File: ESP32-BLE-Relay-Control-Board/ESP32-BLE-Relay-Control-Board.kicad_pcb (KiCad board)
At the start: 2 copper layers, 37 x 90 mm, 37 parts, among them J1 Screw_Terminal_01x02, J2 Screw_Terminal_01x02, J3 Screw_Terminal_01x02, J4 Screw_Terminal_01x02, J5 Conn_01x06_Female, K1 SANYOU_SRD_Form_C, K2 SANYOU_SRD_Form_C, Q1 BC817, Q2 BC817, U1 ESP32-WROOM-32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

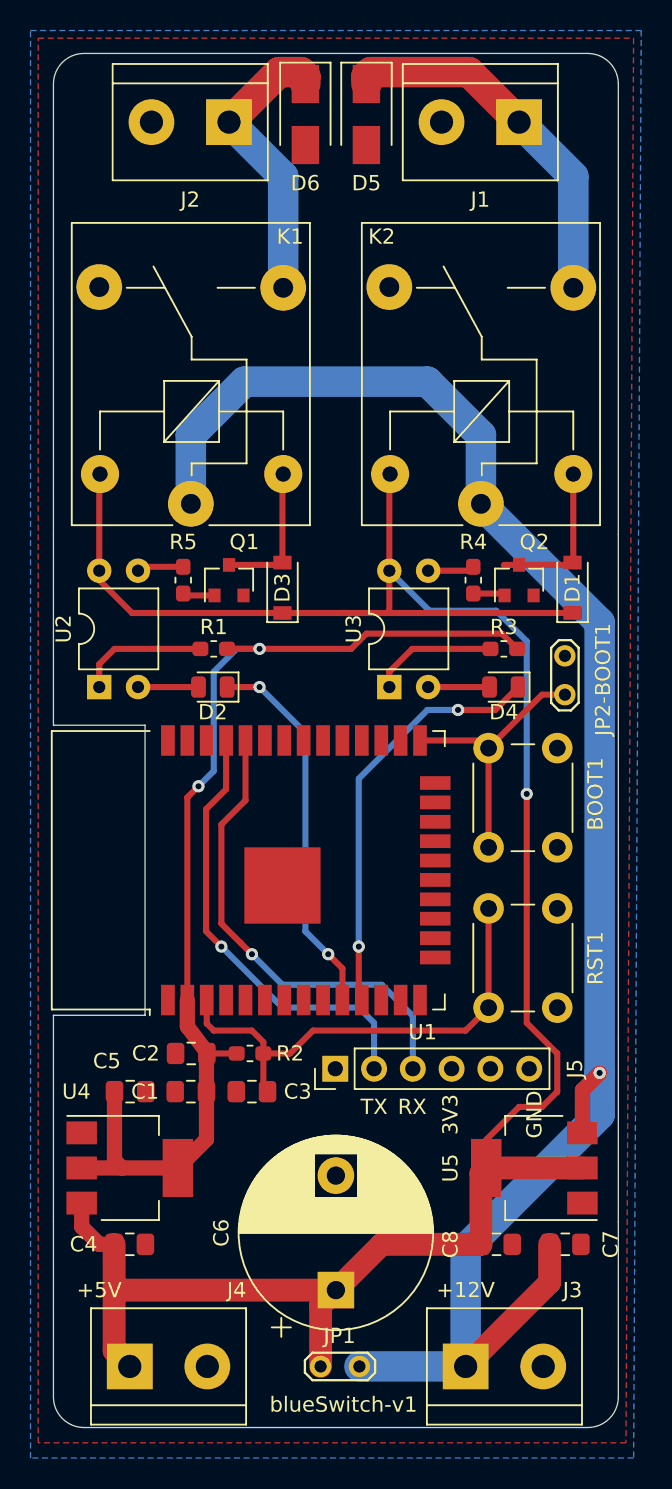
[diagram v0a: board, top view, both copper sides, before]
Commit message: UPDATE, logos added to board
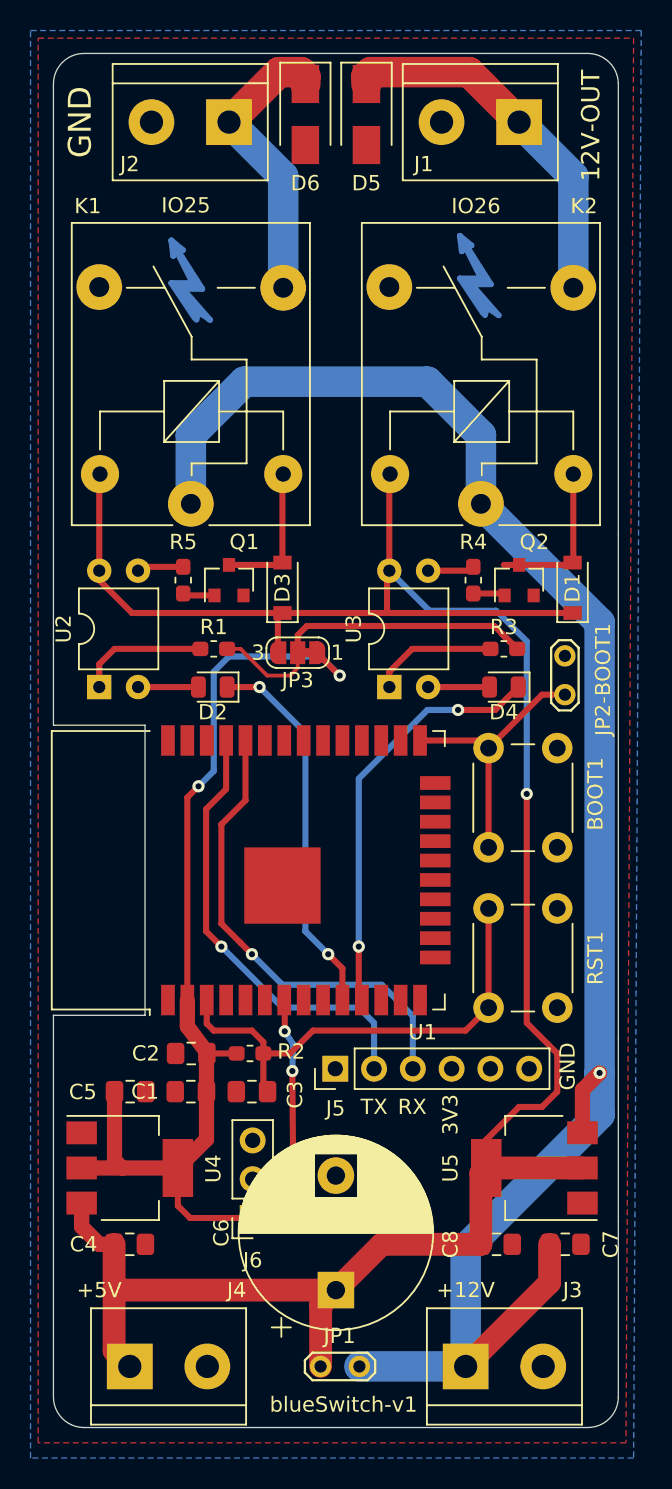
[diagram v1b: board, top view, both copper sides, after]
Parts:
- added J6: Conn_01x03_Male, Connector_PinSocket_2.54mm:PinSocket_1x03_P2.54mm_Vertical, F.Cu at (113.0, 146.3)
- added JP3: Jumper_NC_Dual, Jumper:SolderJumper-3_P1.3mm_Bridged12_RoundedPad1.0x1.5mm_NumberLabels, F.Cu at (116.0, 109.2)
- added REF**: Symbol_Highvoltage_Type1_CopperTop_Small, Symbol:Symbol_Highvoltage_Type1_CopperTop_Small, B.Cu at (127.0, 84.0)
- added REF**: Symbol_Highvoltage_Type1_CopperTop_Small, Symbol:Symbol_Highvoltage_Type1_CopperTop_Small, B.Cu at (108.1, 84.3)
- added REF**: OSHW-Symbol_8.9x8mm_SilkScreen, Symbol:OSHW-Symbol_8.9x8mm_SilkScreen, B.Cu at (129.2, 145.1)
- added REF**: KiCad-Logo2_6mm_SilkScreen, Symbol:KiCad-Logo2_6mm_SilkScreen, B.Cu at (103.9, 142.5)
- C3: value C_Small -> 0.1uF
- R1, R3: value R_Small -> 1K
- R2: value R_Small -> 10K
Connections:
- R1 pad 2: +3V3 -> OPTO_VCC
- R3 pad 2: +3V3 -> OPTO_VCC
- U1 pad 7: Net-(U1-Pad7) -> ADC1_7
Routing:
- net OPTO_VCC: track 0.00 -> 24.4 mm
- net ADC1_7: track 0.00 -> 14.1 mm, vias 0 -> 2
- net +3V3: track 82.6 -> 78.2 mm
- net +5V: track 152.2 -> 154.5 mm
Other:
- board text added: "12V"
- board text added: "12V-OUT"
- board text added: "5V"
- board text added: "IO25"
- board text added: "IO26"
- board text added: "blueSwitch_v1 (12V) 6 Aug 2020 K1 >> IO25 K2 >> IO26 [12V Swtiching Only]"
- board text added: "shridattdudhat.github.io"
